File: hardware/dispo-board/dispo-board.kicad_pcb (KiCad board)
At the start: 4 copper layers, 56.4 x 77.8 mm, 114 parts, among them J1 Conn_01x02, J10 Conn_01x02, J11 Conn_01x03, J12 Conn_01x04, J13 Conn_01x02, J2 Conn_01x02, J3 Conn_ARM_JTAG_SWD_10, J4 Conn_01x02, J5 Conn_01x03, J6 Conn_01x02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

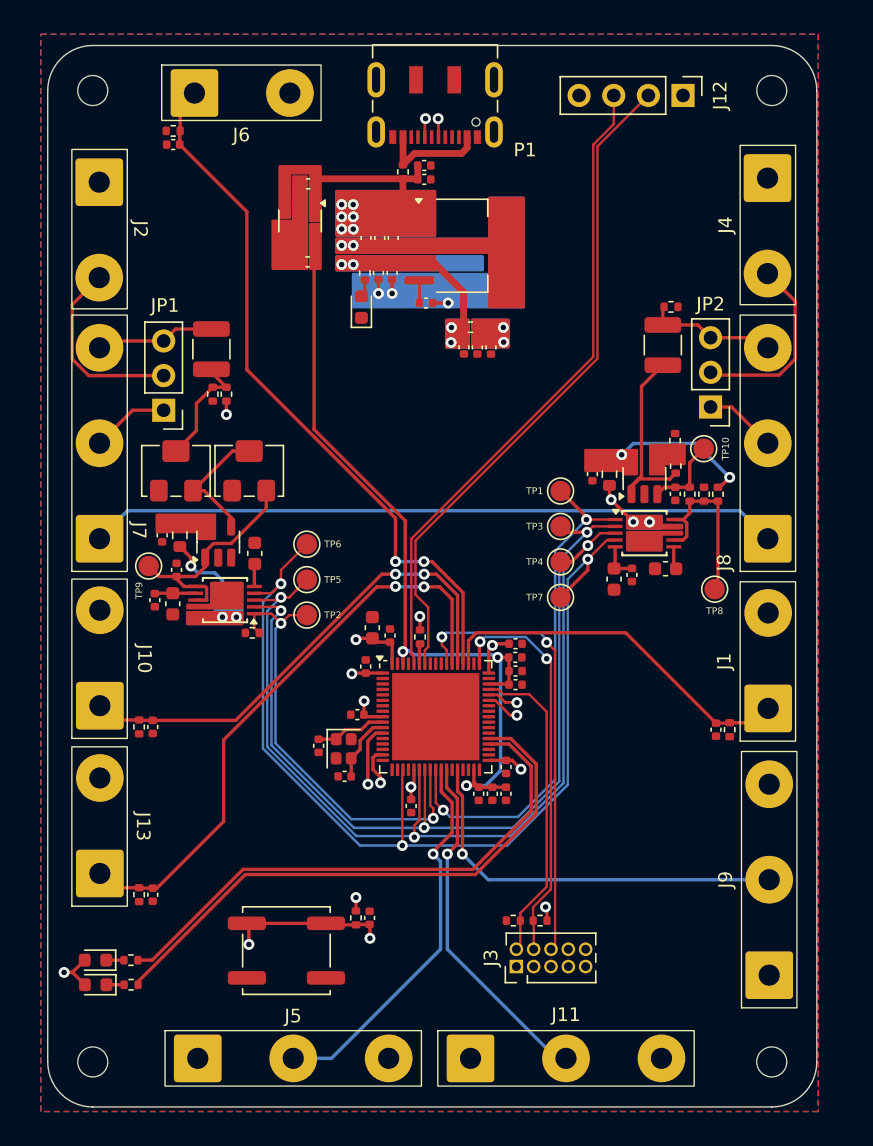
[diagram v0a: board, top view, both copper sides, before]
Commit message: changed again to micro usb, resolved spacing issues
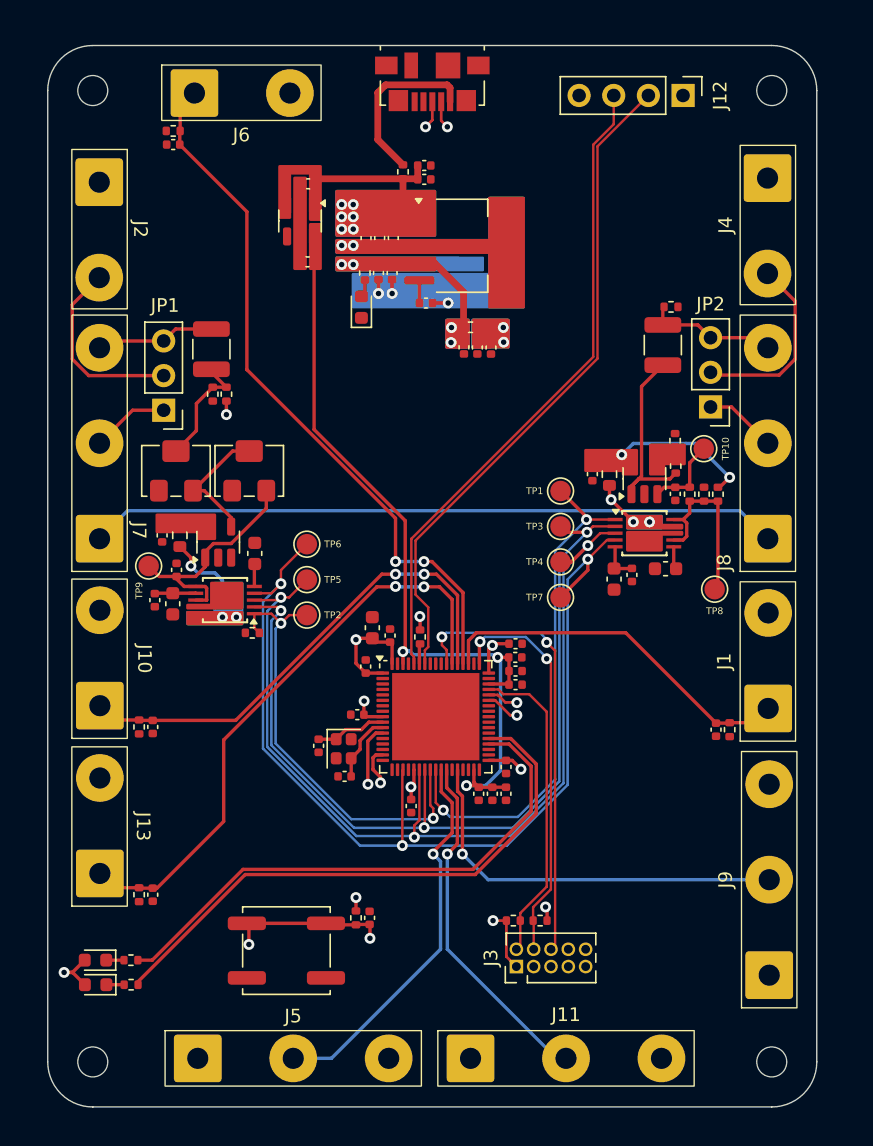
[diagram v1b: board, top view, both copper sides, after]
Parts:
- removed P1: USB_C_Plug_USB2.0, Connector_USB:USB_C_Receptacle_JAE_DX07S016JA1R1500
- added J14: USB_B_Micro, Connector_USB:USB_Micro-B_Molex_47346-0001, F.Cu at (59.7, 26.5)
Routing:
- net +3V3: track 301.1 -> 309.0 mm
- net 5V_USB: track 8.05 -> 12.7 mm
- net USBD-: track 56.5 -> 53.7 mm
- removed copper zone on B.Cu, net GND
- removed copper zone on F.Cu, net GND
- removed copper zone on In1.Cu, net GND
- removed copper zone on In2.Cu, net GND

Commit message: everything connected, ready?
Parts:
- moved C11 0.55 mm to (54.3, 69.6), turned to 180 degrees
- moved TP10 0.51 mm to (80.1, 53.5)
- moved C22 0.51 mm to (74.3, 63.2)
- moved C24 0.51 mm to (73.0, 63.5)
- moved U3 0.51 mm to (75.2, 60.1)
- moved TP8 0.51 mm to (80.3, 64.2)
- moved C25 0.51 mm to (76.8, 62.7)
- moved C12 0.35 mm to (56.2, 67.1)
- moved C13 0.30 mm to (55.0, 66.5)
- moved R1 0.23 mm to (59.0, 67.2)
- moved C9 0.17 mm to (58.1, 79.4)
- moved R12 0.05 mm to (80.6, 56.7)
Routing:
- net GND: track 4.19 -> 52.7 mm, vias 6 -> 184
- net +5V: track 12.5 -> 15.6 mm
- net Net-(U4-OUT): track 14.6 -> 13.4 mm
- net LED_STATUS1: track 40.4 -> 41.5 mm
- net LED_STATUS2: track 42.4 -> 43.4 mm
- net Net-(U4-V+): track 10.5 -> 9.51 mm
- net +3.3VA: track 182.1 -> 181.2 mm
- net SWCLK: track 29.3 -> 30.1 mm
- net I2S6_SDO: track 38.1 -> 38.7 mm
- net ADC1_INP8: track 25.8 -> 25.2 mm
- added copper zone on B.Cu, net GND
- added copper zone on F.Cu, net GND
- added copper zone on In1.Cu, net GND
- added copper zone on In2.Cu, net GND

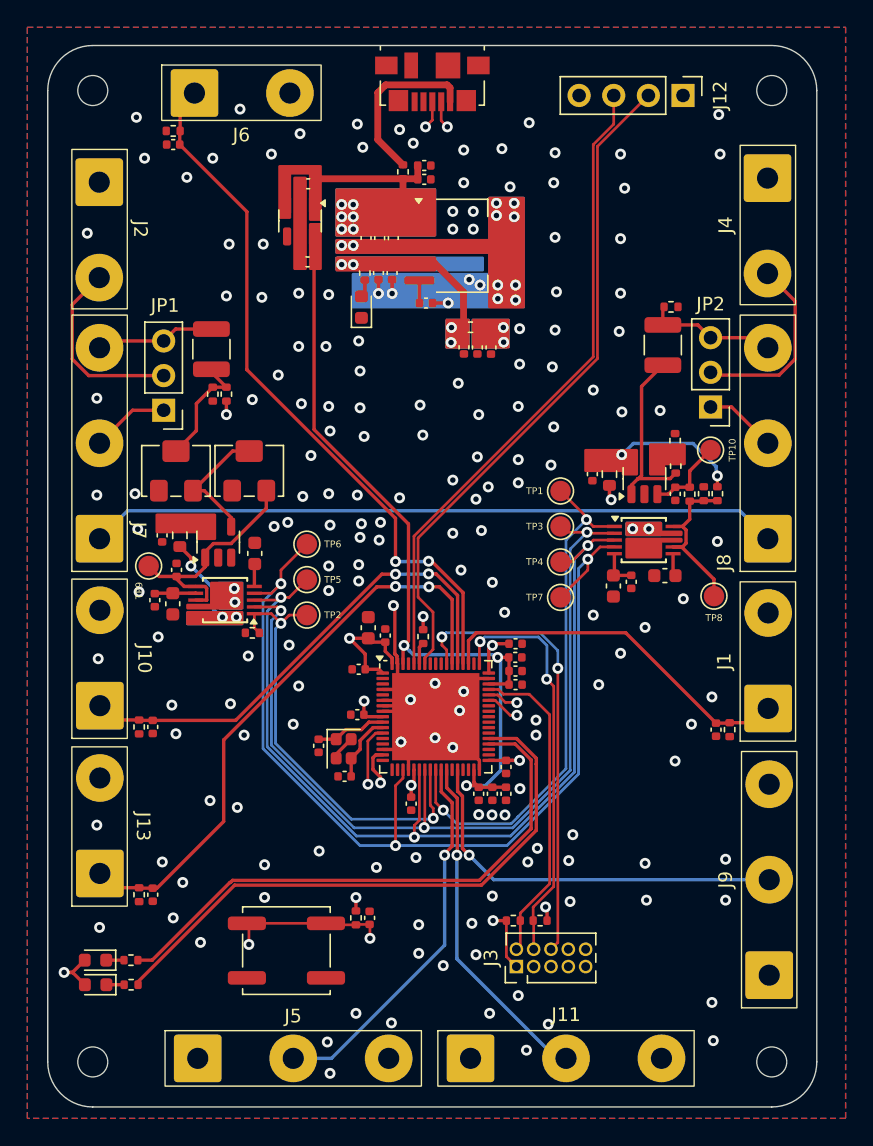
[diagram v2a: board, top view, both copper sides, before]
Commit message: changed text sizes, some other stuff
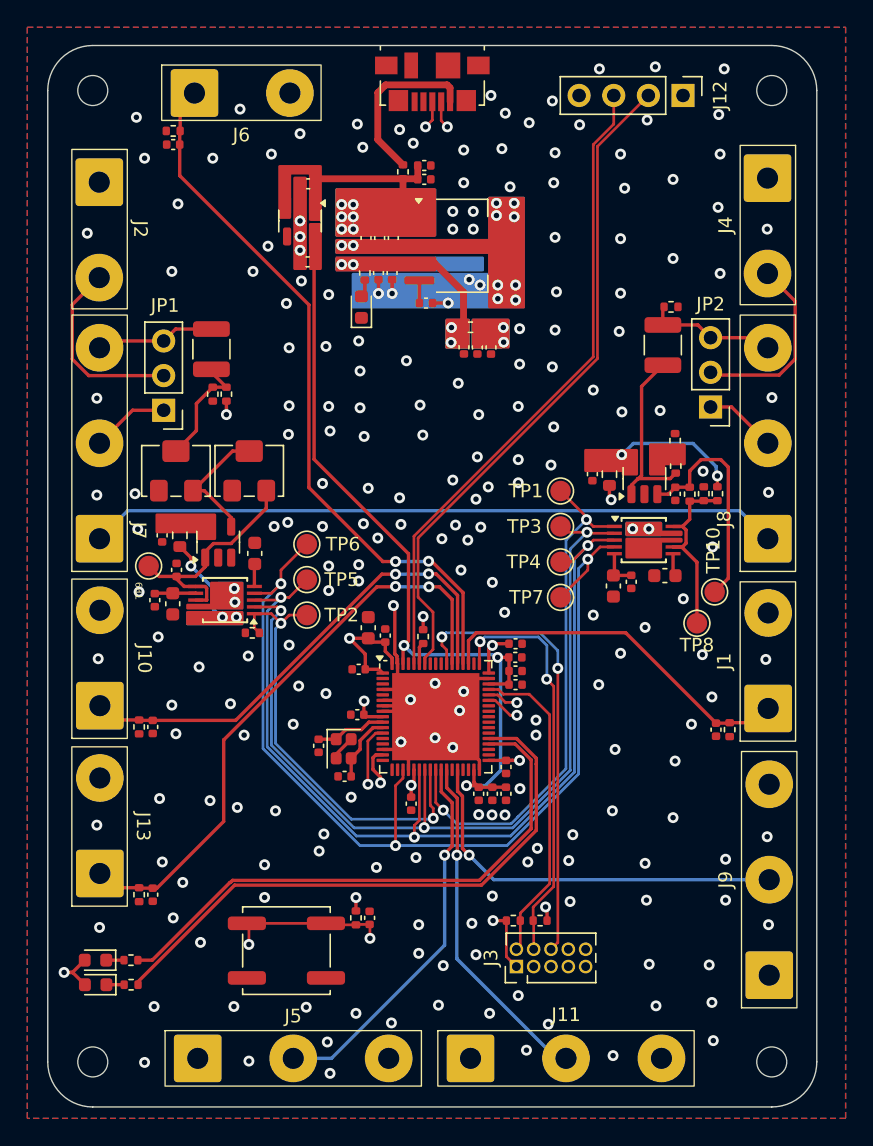
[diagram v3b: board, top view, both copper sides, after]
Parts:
- moved TP10 10.4 mm to (80.4, 63.9)
- moved TP8 2.35 mm to (79.1, 66.2)
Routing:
- net Net-(U4-+): track 5.95 -> 16.7 mm
- net Net-(U3-AOUTL): track 12.8 -> 14.0 mm
- net DIG_IN2: track 52.7 -> 53.2 mm
- net GND: vias 184 -> 225

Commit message: added some text, minor changes, should be ready for production
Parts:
- moved JP2 1.71 mm to (78.4, 50.5)
- moved R19 1.67 mm to (75.5, 43.2)
- moved C31 1.67 mm to (75.0, 46.0)
- moved C32 1.50 mm to (45.0, 46.0)
- moved R20 1.50 mm to (46.1, 49.3)
- moved R21 1.50 mm to (45.1, 49.3)
- moved JP1 1.45 mm to (41.5, 50.6)
- moved R18 1.10 mm to (78.5, 53.2), turned to 0 degrees
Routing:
- net GUITAR_OUT: track 13.9 -> 16.3 mm
- net GUITAR_OUT_µC: track 10.7 -> 13.1 mm
- net GUITAR_IN: track 14.0 -> 16.1 mm
- net GUITAR_OUT_switch: track 5.30 -> 6.92 mm
- net GUITAR_IN_µC: track 8.77 -> 10.3 mm
- net GUITAR_IN_switch: track 5.70 -> 7.15 mm
- net +3.3VA: track 181.2 -> 179.8 mm
- net Net-(C32-Pad1): track 8.58 -> 9.66 mm
- net Net-(U4-OUT): track 13.4 -> 12.5 mm
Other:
- board text added: "IN"
- board text added: "OUT"
- board text added: "bp switch"
